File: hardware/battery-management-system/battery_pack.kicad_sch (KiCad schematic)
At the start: 28 parts, among them J1 CELL4_PLUS, J2 CELL4_MINUS, J24 Charge, J25 Discharge, J3 CELL3_MINUS, J4 CELL2_MINUS, J5 CELL1_MINUS, J6 VBAT+, J7 VBAT+_CHARGE, J8 VBAT-, Q1 DMN3404L, Q2 TJ40S04M3L, Q3 TJ40S04M3L, Q4 DMN3404L, Q5 DMN3404L

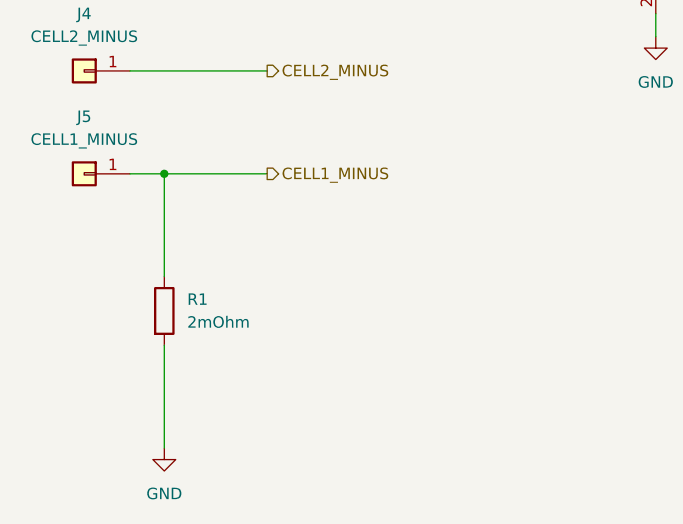
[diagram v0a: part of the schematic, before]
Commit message: start simplifying BMS for R02
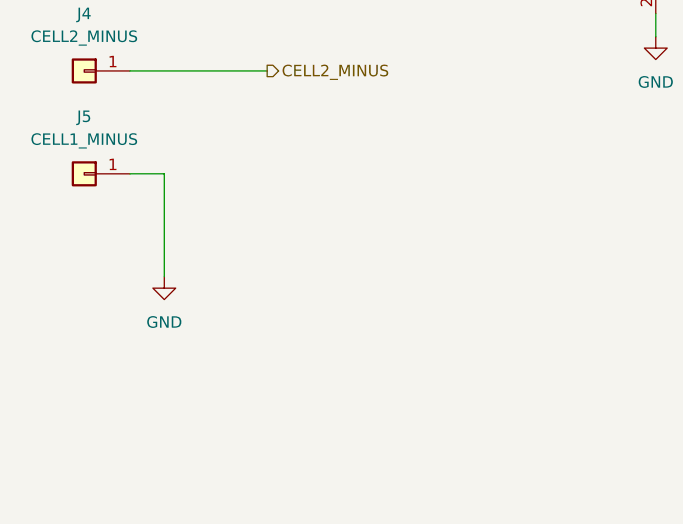
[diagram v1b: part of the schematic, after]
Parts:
- removed R1: 2mOhm, benediktibk:R_2512_6332Metric_Pad1.40x3.35mm_HandSolder, symbol benediktibk:R_2mOhm_SMD_2512_5W_1%
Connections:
- net CELL1_MINUS is gone; now on net GND: J5.1 (Pin_1)
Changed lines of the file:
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@@
   (junction (at 184.15 53.34) (diameter 0) (color 0 0 0 0)
   )
-  (junction (at 40.64 113.03) (diameter 0) (color 0 0 0 0)
-  )
   (junction (at 226.06 86.36) (diameter 0) (color 0 0 0 0)
   )
@@
     (stroke (width 0) (type default))
   )
-  (wire (pts (xy 40.64 132.08) (xy 40.64 143.51))
-    (stroke (width 0) (type default))
-  )
   (wire (pts (xy 144.78 59.69) (xy 144.78 62.23))
     (stroke (width 0) (type default))
   )
   (wire (pts (xy 196.85 76.2) (xy 196.85 77.47))
-    (stroke (width 0) (type default))
-  )
-  (wire (pts (xy 40.64 113.03) (xy 52.07 113.03))
     (stroke (width 0) (type default))
   )
@@
     (effects (font (size 1.27 1.27)) (justify left))
   )
-  (hierarchical_label "CELL1_MINUS" (shape output) (at 52.07 113.03 0) (fields_autoplaced)
-    (effects (font (size 1.27 1.27)) (justify left))
-  )
   (hierarchical_label "CHARGE_AVAILABLE" (shape output) (at 198.12 76.2 0) (fields_autoplaced)
     (effects (font (size 1.27 1.27)) (justify left))
@@
     )
   )
-  (symbol (lib_id "power:GND") (at 40.64 143.51 0) (unit 1)
-    (in_bom yes) (on_board yes) (dnp no) (fields_autoplaced)
-    (property "Reference" "#PWR05" (at 40.64 149.86 0)
-      (effects (font (size 1.27 1.27)) hide)
-    )
-    (property "Value" "GND" (at 40.64 148.59 0)
-      (effects (font (size 1.27 1.27)))
-    )
-    (property "Footprint" "" (at 40.64 143.51 0)
-      (effects (font (size 1.27 1.27)) hide)
-    )
-    (property "Datasheet" "" (at 40.64 143.51 0)
+  (symbol (lib_id "power:GND") (at 40.64 124.46 0) (unit 1)
+    (in_bom yes) (on_board yes) (dnp no) (fields_autoplaced)
+    (property "Reference" "#PWR05" (at 40.64 130.81 0)
+      (effects (font (size 1.27 1.27)) hide)
+    )
+    (property "Value" "GND" (at 40.64 129.54 0)
+      (effects (font (size 1.27 1.27)))
+    )
+    (property "Footprint" "" (at 40.64 124.46 0)
+      (effects (font (size 1.27 1.27)) hide)
+    )
+    (property "Datasheet" "" (at 40.64 124.46 0)
       (effects (font (size 1.27 1.27)) hide)
     )
@@
         )
       )
-    )
-  )
-  (symbol (lib_id "benediktibk:R_2mOhm_SMD_2512_5W_1%") (at 40.64 128.27 0) (unit 1)
-    (in_bom yes) (on_board yes) (dnp no) (fields_autoplaced)
-    (property "Reference" "R1" (at 43.18 126.9999 0)
-      (effects (font (size 1.27 1.27)) (justify left))
-    )
-    (property "Value" "2mOhm" (at 43.18 129.5399 0)
-      (effects (font (size 1.27 1.27)) (justify left))
-    )
-    (property "Footprint" "benediktibk:R_2512_6332Metric_Pad1.40x3.35mm_HandSolder" (at 30.48 127.762 90)
-      (effects (font (size 1.27 1.27)) hide)
-    )
-    (property "Datasheet" "~" (at 40.64 128.27 0)
-      (effects (font (size 1.27 1.27)) hide)
-    )
-    (property "RS order number" "231-3683" (at 22.86 127 0)
-      (effects (font (size 1.27 1.27)) hide)
-    )
-    (pin "1")
-    (pin "2")
-    (instances
-      (project "battery-management-system"
-        (path "/5272f0ff-3069-41a9-bca2-80beede8b4b2/31b87c35-c096-4dc0-8978-834bec283b57"
-          (reference "R1") (unit 1)
-        )
-      )

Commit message: fix design errors
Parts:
- added R1, R3: 220kOhm, benediktibk:R_0603_1608Metric_Pad0.98x0.95mm_HandSolder, symbol benediktibk:R_220kOhm_SMD_0603_100mW_1%
- renumbered J8 to J10, J24 to J6, J25 to J7, J6 to J8, J7 to J9, R3 to R4, R4 to R5, R5 to R6
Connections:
- net CHARGE: now also R1.1
- net DISCHARGE: now also R3.1
- net GND: now also R1.2, R3.2

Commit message: fix design errors
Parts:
- removed D5, D6: SBR2065D1, benediktibk:SBR2065D1, symbol benediktibk:SBR2065D1
- removed J1: CELL4_PLUS, benediktibk:Connector_M6, symbol benediktibk:Connector_M6
- removed J10: VBAT-, benediktibk:Connector_M6, symbol benediktibk:Connector_M6
- removed J2: CELL4_MINUS, benediktibk:Connector_M6, symbol benediktibk:Connector_M6
- removed J3: CELL3_MINUS, benediktibk:Connector_M6, symbol benediktibk:Connector_M6
- removed J4: CELL2_MINUS, benediktibk:Connector_M6, symbol benediktibk:Connector_M6
- removed J5: CELL1_MINUS, benediktibk:Connector_M6, symbol benediktibk:Connector_M6
- removed J8: VBAT+, benediktibk:Connector_M6, symbol benediktibk:Connector_M6
- removed J9: VBAT+_CHARGE, benediktibk:Connector_M6, symbol benediktibk:Connector_M6
- added J1: CELLS, benediktibk:rspro_header_5pin_5_08mm, symbol benediktibk:rspro_header_5pin_5_08mm
- added J2: VBAT_DISCHARGE, benediktibk:rspro_header_2pin_5_08mm, symbol benediktibk:rspro_header_2pin_5_08mm
- added J3: VBAT_CHARGE, benediktibk:rspro_header_2pin_5_08mm, symbol benediktibk:rspro_header_2pin_5_08mm
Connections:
- net CELL2_MINUS: now also J1.4 (Pin_4)
- net CELL3_MINUS: now also J1.3 (Pin_3)
- net CELL4_MINUS: now also J1.2 (Pin_2)
- net GND: now also J1.5 (Pin_5), J2.2 (Pin_2), J3.2 (Pin_2)
- net PACK: now also J1.1 (Pin_1)
- net at F1.1: now also J2.1 (Pin_1)
- net at F2.1: now also J3.1 (Pin_1)

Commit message: fix design errors
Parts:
- renumbered J6 to J2, J7 to J3, J2 to J4, J3 to J5
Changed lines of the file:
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@@
   (symbol (lib_id "benediktibk:rspro_header_2pin_5_08mm") (at 262.89 43.18 0) (unit 1)
     (in_bom yes) (on_board yes) (dnp no) (fields_autoplaced)
-    (property "Reference" "J2" (at 266.7 44.45 0)
+    (property "Reference" "J4" (at 266.7 44.45 0)
       (effects (font (size 1.27 1.27)) (justify left))
     )
@@
       (project "battery-management-system"
         (path "/5272f0ff-3069-41a9-bca2-80beede8b4b2/31b87c35-c096-4dc0-8978-834bec283b57"
-          (reference "J2") (unit 1)
+          (reference "J4") (unit 1)
         )
       )
@@
   (symbol (lib_id "benediktibk:Conn_01x02") (at 106.68 73.66 0) (unit 1)
     (in_bom yes) (on_board yes) (dnp no) (fields_autoplaced)
-    (property "Reference" "J6" (at 110.49 74.93 0)
+    (property "Reference" "J2" (at 110.49 74.93 0)
       (effects (font (size 1.27 1.27)) (justify left))
     )
@@
       (project "battery-management-system"
         (path "/5272f0ff-3069-41a9-bca2-80beede8b4b2/31b87c35-c096-4dc0-8978-834bec283b57"
-          (reference "J6") (unit 1)
+          (reference "J2") (unit 1)
         )
       )
@@
   (symbol (lib_id "benediktibk:rspro_header_2pin_5_08mm") (at 262.89 52.07 0) (unit 1)
     (in_bom yes) (on_board yes) (dnp no) (fields_autoplaced)
-    (property "Reference" "J3" (at 266.7 53.34 0)
+    (property "Reference" "J5" (at 266.7 53.34 0)
       (effects (font (size 1.27 1.27)) (justify left))
     )
@@
       (project "battery-management-system"
         (path "/5272f0ff-3069-41a9-bca2-80beede8b4b2/31b87c35-c096-4dc0-8978-834bec283b57"
-          (reference "J3") (unit 1)
+          (reference "J5") (unit 1)
         )
       )
@@
   (symbol (lib_id "power:GND") (at 256.54 58.42 0) (unit 1)
     (in_bom yes) (on_board yes) (dnp no) (fields_autoplaced)
-    (property "Reference" "#PWR067" (at 256.54 64.77 0)
+    (property "Reference" "#PWR012" (at 256.54 64.77 0)
       (effects (font (size 1.27 1.27)) hide)
     )
@@
       (project "battery-management-system"
         (path "/5272f0ff-3069-41a9-bca2-80beede8b4b2/31b87c35-c096-4dc0-8978-834bec283b57"
-          (reference "#PWR067") (unit 1)
+          (reference "#PWR012") (unit 1)
         )
       )
@@
   (symbol (lib_id "benediktibk:Conn_01x02") (at 157.48 73.66 0) (unit 1)
     (in_bom yes) (on_board yes) (dnp no) (fields_autoplaced)
-    (property "Reference" "J7" (at 161.29 74.93 0)
+    (property "Reference" "J3" (at 161.29 74.93 0)
       (effects (font (size 1.27 1.27)) (justify left))
     )
@@
       (project "battery-management-system"
         (path "/5272f0ff-3069-41a9-bca2-80beede8b4b2/31b87c35-c096-4dc0-8978-834bec283b57"
-          (reference "J7") (unit 1)
-        )
-      )
+          (reference "J3") (unit 1)
+        )
+      )

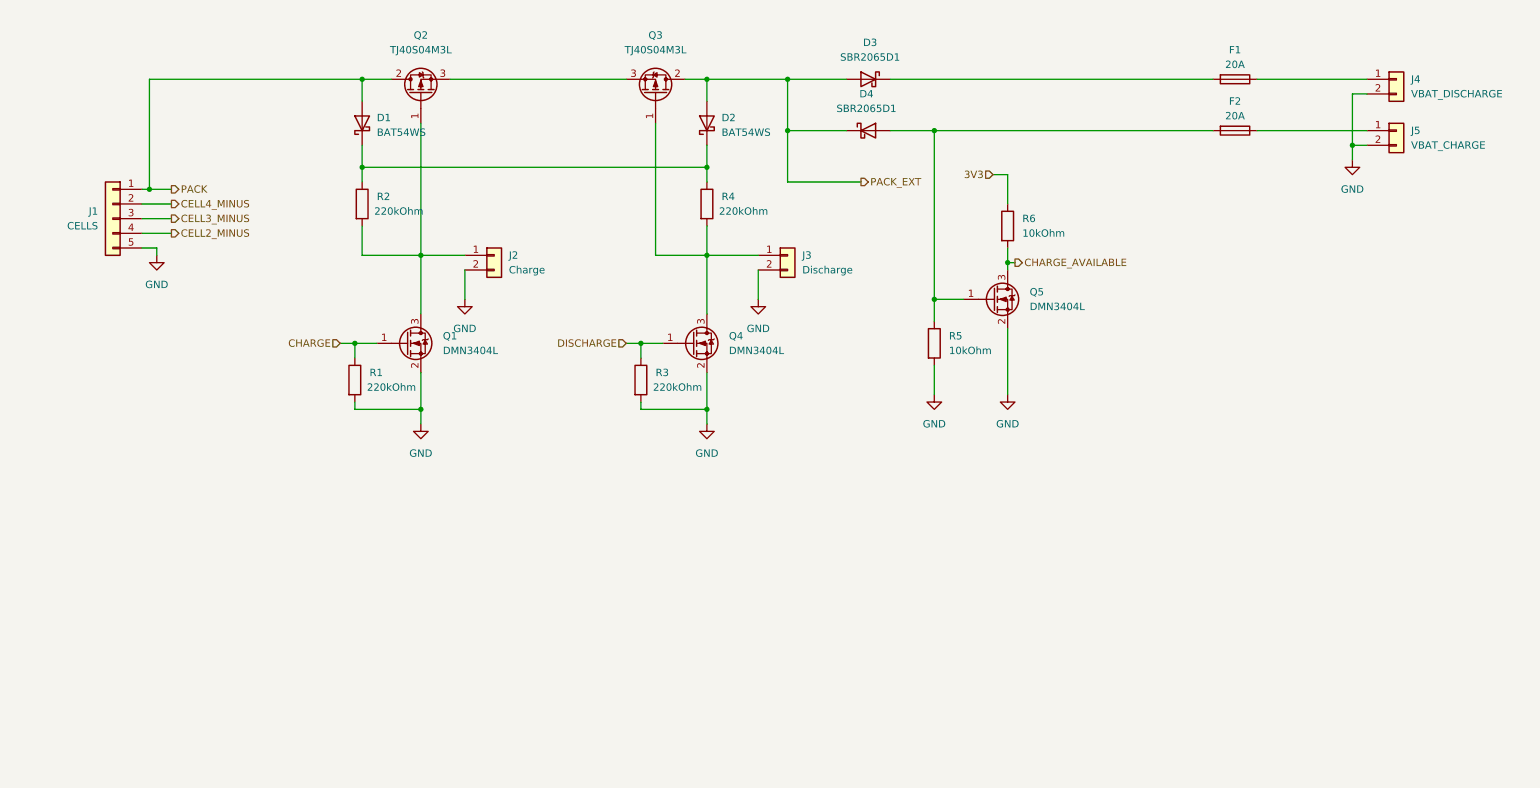
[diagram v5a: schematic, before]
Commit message: add fuel gauge to BMS
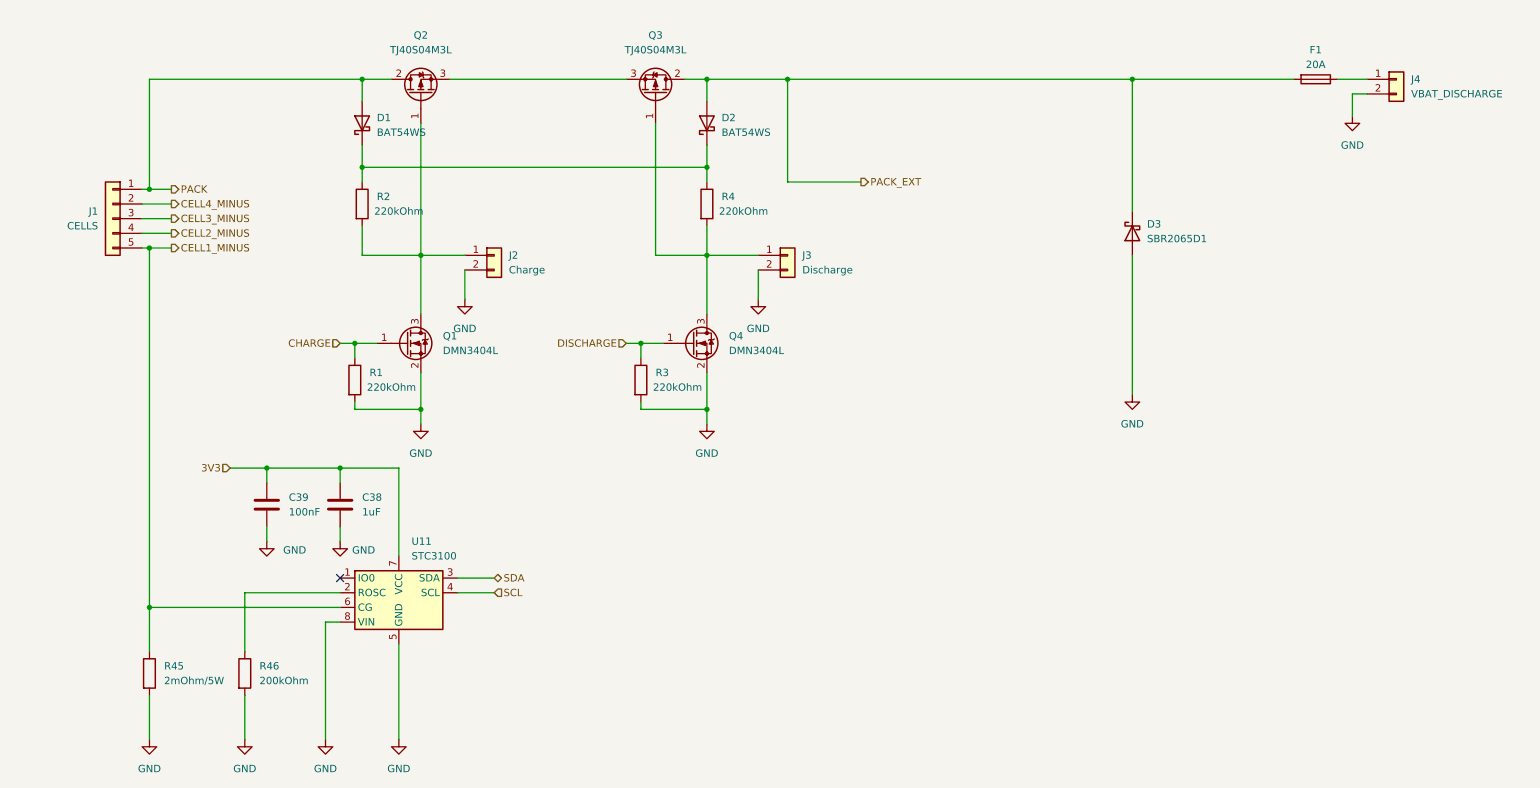
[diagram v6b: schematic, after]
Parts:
- removed D4: SBR2065D1, benediktibk:SBR2065D1, symbol benediktibk:SBR2065D1
- removed F2: 20A, benediktibk:KEYSTONE_blade_fus_holder, symbol benediktibk:KEYSTONE_blade_fuse_holder
- removed J5: VBAT_CHARGE, benediktibk:rspro_header_2pin_5_08mm, symbol benediktibk:rspro_header_2pin_5_08mm
- removed Q5: DMN3404L, benediktibk:SOT-23, symbol benediktibk:DMN3404L
- removed R5, R6: 10kOhm, benediktibk:R_0603_1608Metric_Pad0.98x0.95mm_HandSolder, symbol benediktibk:R_10kOhm_SMD_0603_100mW_1%
- added C38: 1uF, benediktibk:C_0603_1608Metric_Pad1.08x0.95mm_HandSolder, symbol benediktibk:C_1uF_SMD_0603_50V_10%
- added C39: 100nF, benediktibk:C_0603_1608Metric_Pad1.08x0.95mm_HandSolder, symbol benediktibk:C_100nF_SMD_0603_50V
- added R45: 2mOhm/5W, benediktibk:R_2512_6332Metric_Pad1.40x3.35mm_HandSolder, symbol benediktibk:R_2mOhm_SMD_2512_5W_1%
- added R46: 200kOhm, benediktibk:R_0603_1608Metric_Pad0.98x0.95mm_HandSolder, symbol benediktibk:R_200kOhm_SMD_0603_30mW_0_1%
- added U11: STC3100, benediktibk:MSOP-8_3x3mm_P0.65mm, symbol benediktibk:STC3100
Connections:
- net 3V3: now also C38.1, C39.1, U11.7 (VCC)
- net GND: now also D3.1 (A), C38.2, C39.2, R45.2, R46.2, U11.5 (GND), U11.8 (VIN); no longer J1.5 (Pin_5)
- net PACK_EXT: now also D3.2 (K), F1.2; no longer D3.1 (A)
- new net: R46.1, U11.2 (ROSC)
- new net CELL1_MINUS: J1.5 (Pin_5), R45.1, U11.6 (CG)
- new net SCL: U11.4 (SCL)
- new net SDA: U11.3 (SDA)
- no-connect marks 0 -> 1
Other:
- moved on the sheet: D3, F1

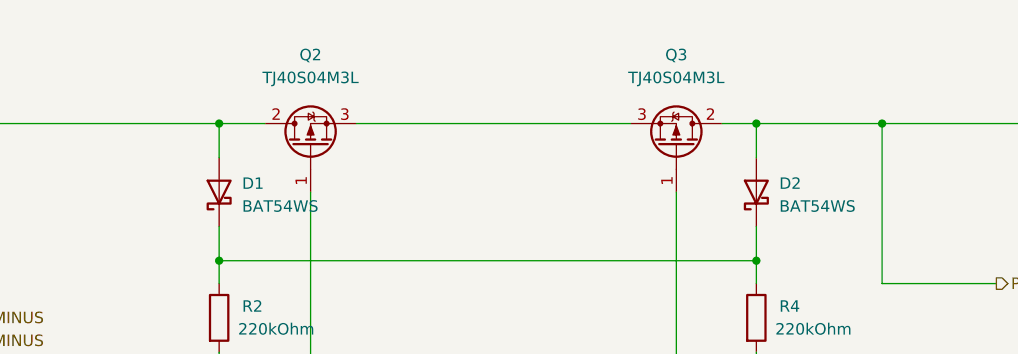
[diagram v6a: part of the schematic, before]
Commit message: fix design errors of battery management system R02
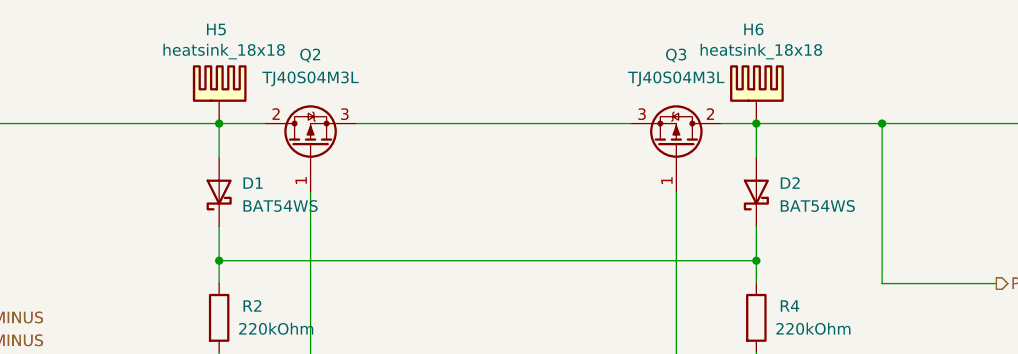
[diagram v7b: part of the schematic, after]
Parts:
- added H5, H6: heatsink_18x18, benediktibk:heatsink_18x18, symbol benediktibk:heatsink_18x18
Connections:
- net PACK: now also H5.PAD
- net PACK_EXT: now also H6.PAD
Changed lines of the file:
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@@
+	(wire
+		(pts
+			(xy 100.33 44.45) (xy 130.81 44.45)
+		)
+		(stroke
+			(width 0)
+			(type default)
+		)
+	)
 	(wire
 		(pts
@@
 		(pts
 			(xy 140.97 44.45) (xy 144.78 44.45)
-		)
-		(stroke
-			(width 0)
-			(type default)
-		)
-	)
-	(wire
-		(pts
-			(xy 100.33 44.45) (xy 130.81 44.45)
 		)
 		(stroke
@@
 	)
 	(symbol
+		(lib_id "benediktibk:heatsink_18x18")
+		(at 144.78 40.64 0)
+		(unit 1)
+		(exclude_from_sim no)
+		(in_bom yes)
+		(on_board yes)
+		(dnp no)
+		(property "Reference" "H6"
+			(at 143.256 34.036 0)
+			(effects
+				(font
+					(size 1.27 1.27)
+				)
+				(justify left)
+			)
+		)
+		(property "Value" "heatsink_18x18"
+			(at 138.43 36.322 0)
+			(effects
+				(font
+					(size 1.27 1.27)
+				)
+				(justify left)
+			)
+		)
+		(property "Footprint" "benediktibk:heatsink_18x18"
+			(at 144.907 30.734 0)
+			(effects
+				(font
+					(size 1.27 1.27)
+				)
+				(hide yes)
+			)
+		)
+		(property "Datasheet" "~"
+			(at 144.78 33.02 0)
+			(effects
+				(font
+					(size 1.27 1.27)
+				)
+				(hide yes)
+			)
+		)
+		(property "Description" ""
+			(at 144.526 40.64 0)
+			(effects
+				(font
+					(size 1.27 1.27)
+				)
+				(hide yes)
+			)
+		)
+		(property "Mouser order number" "490-HSB06-181810"
+			(at 145.288 34.798 0)
+			(effects
+				(font
+					(size 1.27 1.27)
+				)
+				(hide yes)
+			)
+		)
+		(pin "PAD"
+		)
+		(instances
+			(project "battery-management-system"
+				(path "/5272f0ff-3069-41a9-bca2-80beede8b4b2/31b87c35-c096-4dc0-8978-834bec283b57"
+					(reference "H6")
+					(unit 1)
+				)
+			)
+		)
+	)
+	(symbol
 		(lib_id "benediktibk:DMN3404L")
 		(at 92.71 90.17 0)
@@
 					(unit 1)
 				)
+			)
+		)
+	)
+	(symbol
+		(lib_id "benediktibk:heatsink_18x18")
+		(at 85.09 40.64 0)
+		(unit 1)
+		(exclude_from_sim no)
+		(in_bom yes)
+		(on_board yes)
+		(dnp no)
+		(property "Reference" "H5"
+			(at 83.566 34.036 0)
+			(effects
+				(font
+					(size 1.27 1.27)
+				)
+				(justify left)
+			)
+		)
+		(property "Value" "heatsink_18x18"
+			(at 78.74 36.322 0)
+			(effects
+				(font
+					(size 1.27 1.27)
+				)
+				(justify left)
+			)
+		)
+		(property "Footprint" "benediktibk:heatsink_18x18"
+			(at 85.217 30.734 0)
+			(effects
+				(font
+					(size 1.27 1.27)
+				)
+				(hide yes)
+			)
+		)
+		(property "Datasheet" "~"
+			(at 85.09 33.02 0)
+			(effects
+				(font
+					(size 1.27 1.27)
+				)
+				(hide yes)
+			)
+		)
+		(property "Description" ""
+			(at 84.836 40.64 0)
+			(effects
+				(font
+					(size 1.27 1.27)
+				)
+				(hide yes)
+			)
+		)
+		(property "Mouser order number" "490-HSB06-181810"
+			(at 85.598 34.798 0)
+			(effects
+				(font
+					(size 1.27 1.27)
+				)
+				(hide yes)
+			)
+		)
+		(pin "PAD"
+		)
+		(instances
+			(project "battery-management-system"
+				(path "/5272f0ff-3069-41a9-bca2-80beede8b4b2/31b87c35-c096-4dc0-8978-834bec283b57"
+					(reference "H5")
+					(unit 1)
+				)
